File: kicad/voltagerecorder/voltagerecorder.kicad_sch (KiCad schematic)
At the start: 35 parts

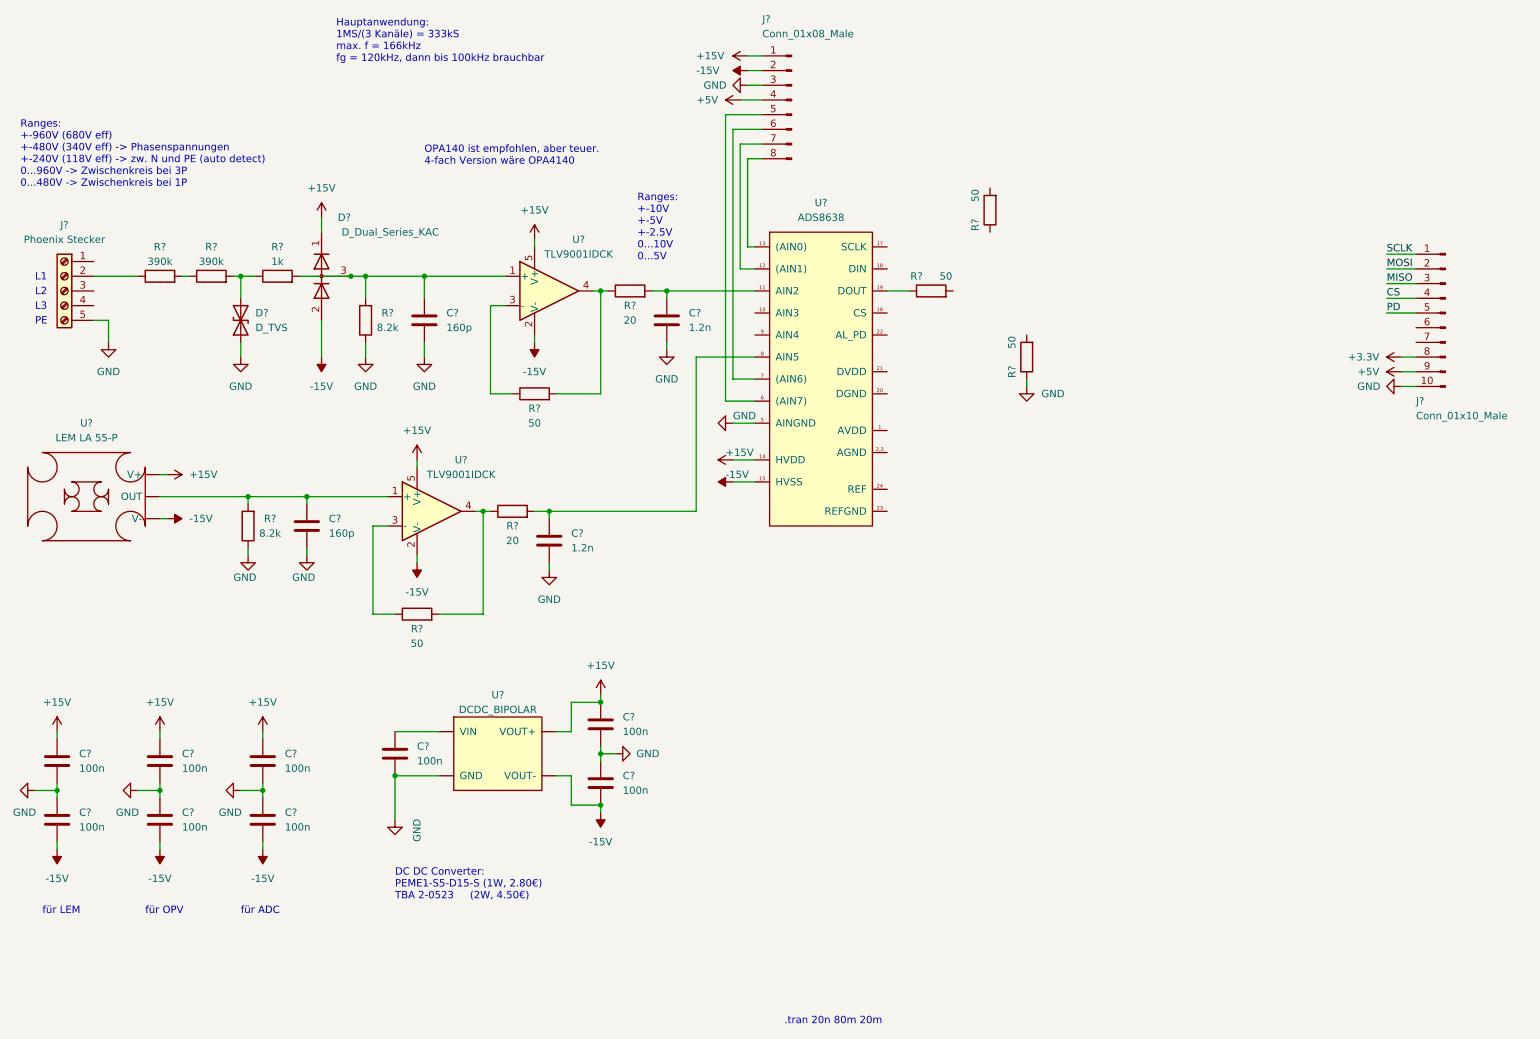
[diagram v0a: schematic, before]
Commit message: Schaltplan auf Hierachisch umgestellt.
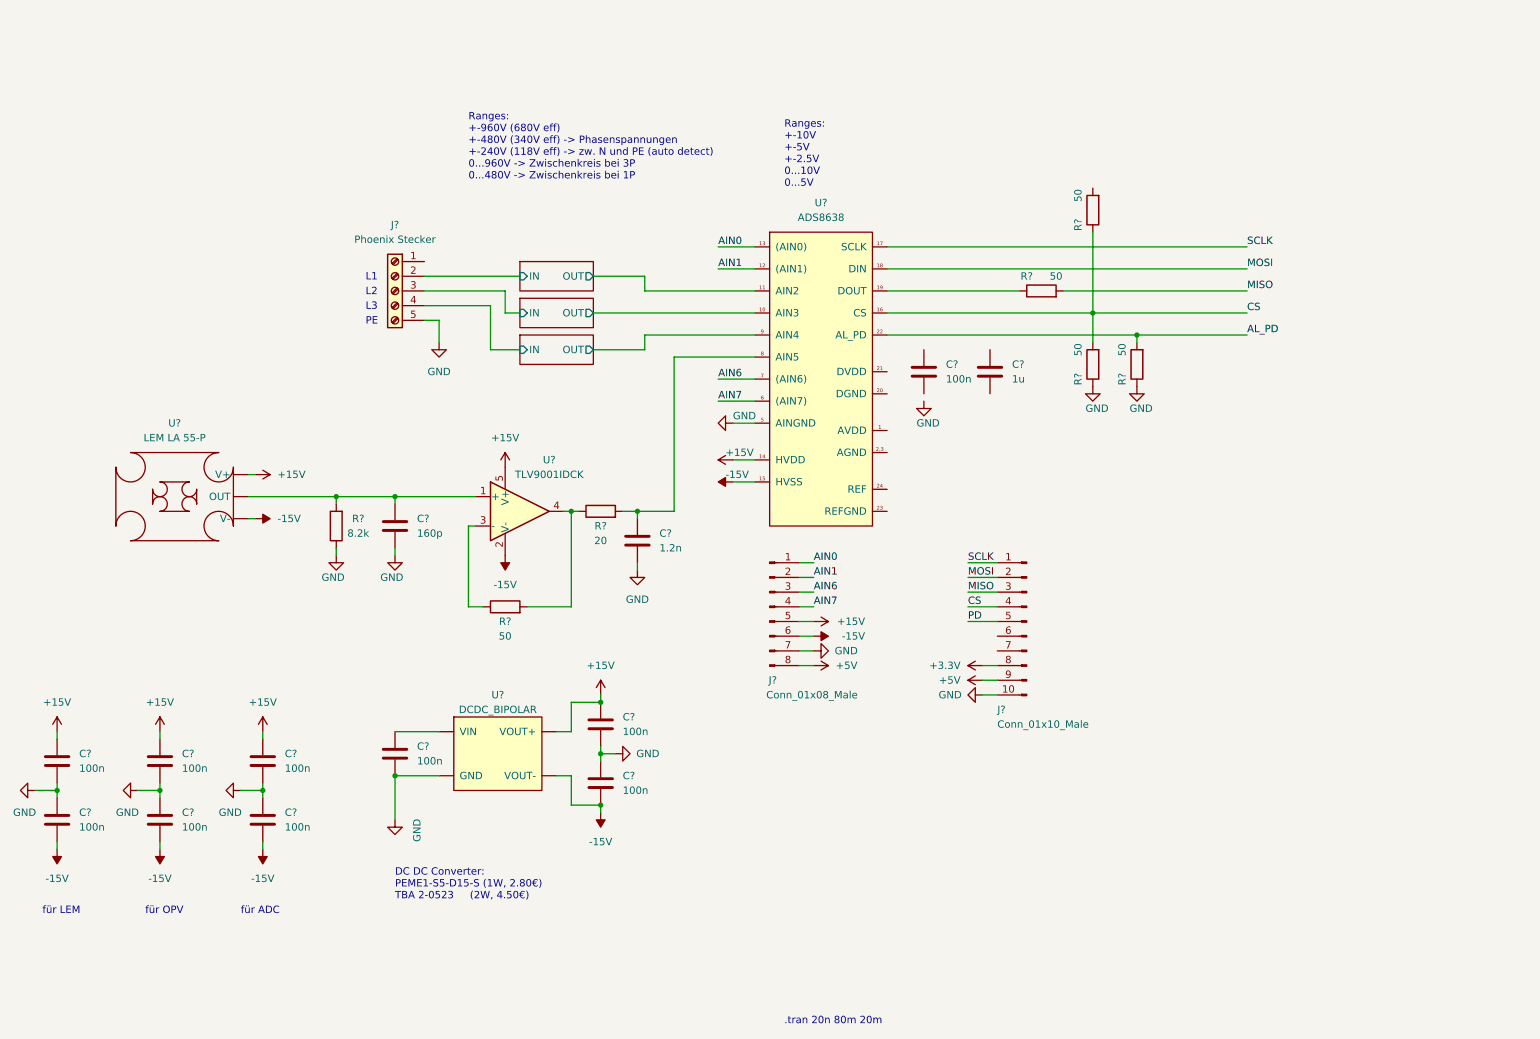
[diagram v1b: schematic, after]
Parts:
- removed C?: 1.2n, symbol Device:C
- removed C?: 160p, symbol Device:C
- removed D?: D_Dual_Series_KAC, symbol Device:D_Dual_Series_KAC
- removed D?: D_TVS, symbol Device:D_TVS
- removed R?: 8.2k, symbol Device:R
- removed R?: 20, symbol Device:R
- removed R?: 1k, symbol Device:R
- removed R? (x2): 390k, symbol Device:R
- removed R?: 50, symbol Device:R
- removed U?: TLV9001IDCK, Package_TO_SOT_SMD:SOT-353_SC-70-5, symbol Amplifier_Operational:TLV9001IDCK
- added C?: 1u, symbol Device:C
- added C?: 100n, symbol Device:C
- added R?: 50, symbol Device:R
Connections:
- net +15V: now also J?.5 (Pin_5); no longer J?.1 (Pin_1)
- net +5V: now also J?.8 (Pin_8); no longer J?.4 (Pin_4)
- net -15V: now also J?.6 (Pin_6); no longer J?.2 (Pin_2)
- net CS: now also R?.1, U?.16 (CS), R?.2
- net GND: now also J?.7 (Pin_7), R?.1; no longer J?.3 (Pin_3)
- net MISO: now also R?.2
- net MOSI: now also U?.18 (DIN)
- net SCLK: now also U?.17 (SCLK)
- net voltage_input/OUT: now reaches U?.11 (AIN2)
- net voltage_input/IN: now reaches J?.2 (Pin_2)
- net voltage_input1/IN: now reaches J?.3 (Pin_3)
- net voltage_input2/IN: now reaches J?.4 (Pin_4)
- net AL_PD: now reaches R?.2
- net AL_PD: now also U?.22 (AL_PD)
- net AIN7: now reaches U?.6 ((AIN7))
- net AIN7: now also J?.4 (Pin_4); no longer J?.5 (Pin_5)
- net AIN6: now reaches U?.7 ((AIN6))
- net AIN6: now also J?.3 (Pin_3); no longer J?.6 (Pin_6)
- net AIN1: now reaches U?.12 ((AIN1))
- net AIN1: now also J?.2 (Pin_2); no longer J?.7 (Pin_7)
- net AIN0: now reaches U?.13 ((AIN0))
- net AIN0: now also J?.1 (Pin_1); no longer J?.8 (Pin_8)
- net voltage_input1/OUT: now reaches U?.10 (AIN3)
- net voltage_input2/OUT: now reaches U?.9 (AIN4)
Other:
- added sheet voltage_input (voltage_input.kicad_sch)
- added sheet voltage_input1 (voltage_input.kicad_sch)
- added sheet voltage_input2 (voltage_input.kicad_sch)
- note removed: "Hauptanwendung: 1MS/(3 Kanäle) = 333kS max. f = 166kHz fg = 120kHz, dann bis 100kHz brauchbar"
- note removed: "OPA140 ist empfohlen, aber teuer. 4-fach Version wäre OPA4140"
- moved on the sheet: C?, J?, R?, U?

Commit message: Nach Aufteilung auf Hierachische Schaltpläne.
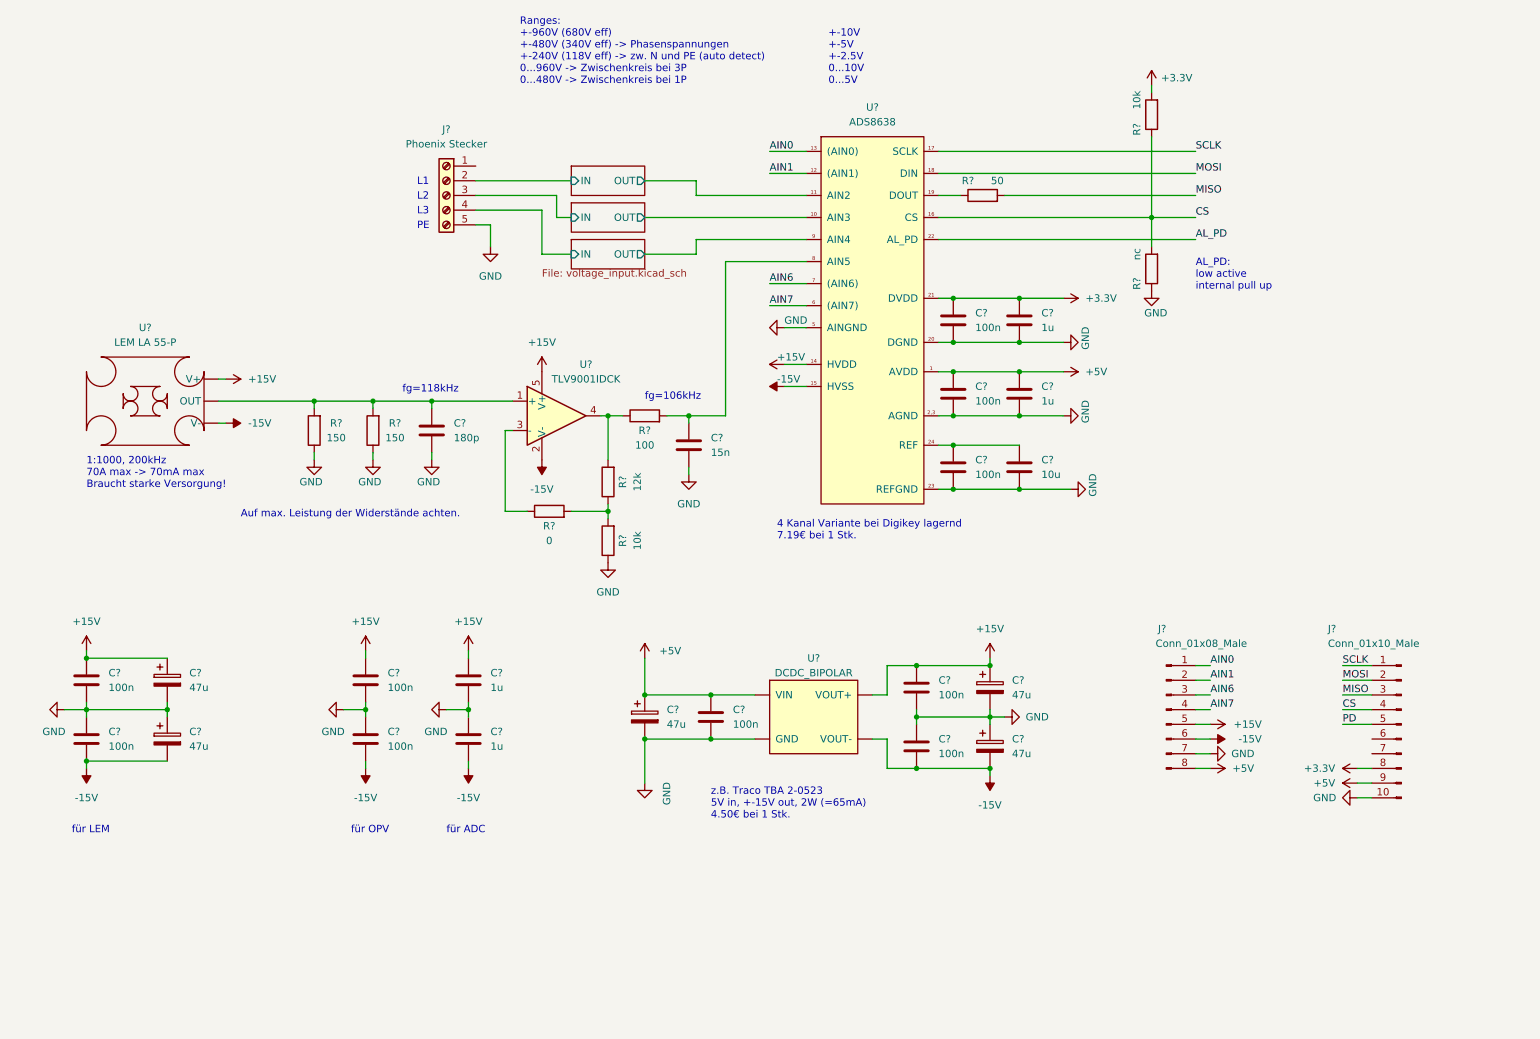
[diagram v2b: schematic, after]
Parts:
- removed R?: 50, symbol Device:R
- added C? (x2): 100n, symbol Device:C
- added C? (x5): 47u, symbol Device:C_Polarized
- added C?: 1u, symbol Device:C
- added C?: 10u, symbol Device:C
- added R?: 12k, symbol Device:R
- added R?: 150, symbol Device:R
- added R?: 10k, symbol Device:R
- C?: value 1.2n -> 15n
- C? (x2): value 100n -> 1u
- C?: value 160p -> 180p
- R?: value 50 -> 10k
- R?: value 50 -> nc
- R?: value 50 -> 0
- R?: value 20 -> 100
- R?: value 8.2k -> 150
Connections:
- net +15V: now also C?.1, C?.1
- net +3.3V: now also C?.1, C?.1, R?.2, U?.21 (DVDD)
- net +5V: now also C?.1, U?. (VOUT-), U?.1 (AVDD), C?.1, C?.1, C?.1
- net -15V: now also C?.2, C?.2
- net GND: now also C?.2, C?.2, U?.2,3 (AGND), U?.20 (DGND), U?.23 (REFGND), C?.1, C?.1, C?.2, C?.2, C?.2, C?.2, C?.2, C?.2, C?.2, R?.1, R?.1
- net at C?.1, R?.2, U?. (V-)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: now also R?.2
- net at R?.1, U?.4: now also R?.2; no longer R?.2
- net at U?.24 (REF): now also C?.1, C?.1
- new net: R?.1, R?.2, R?.2
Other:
- note added: "+-10V +-5V +-2.5V 0...10V 0...5V"
- note added: "1:1000, 200kHz 70A max -> 70mA max Braucht starke Versorgung!"
- note added: "4 Kanal Variante bei Digikey lagernd 7.19€ bei 1 Stk."
- note added: "AL_PD: low active internal pull up"
- note added: "Auf max. Leistung der Widerstände achten."
- note added: "fg=106kHz"
- note added: "fg=118kHz"
- note added: "z.B. Traco TBA 2-0523 5V in, +-15V out, 2W (=65mA) 4.50€ bei 1 Stk."
- note removed: ".tran 20n 80m 20m"
- note removed: "DC DC Converter: PEME1-S5-D15-S (1W, 2.80€) TBA 2-0523 (2W, 4.50€)"
- note removed: "Ranges: +-10V +-5V +-2.5V 0...10V 0...5V"
- moved on the sheet: C?, J?, R?, U?

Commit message: filters changed
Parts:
- C?: value 15n -> 8.2n
- C?: value 180p -> 100p
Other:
- note added: "194kHz"
- note added: "212kHz"
- note removed: "fg=106kHz"
- note removed: "fg=118kHz"

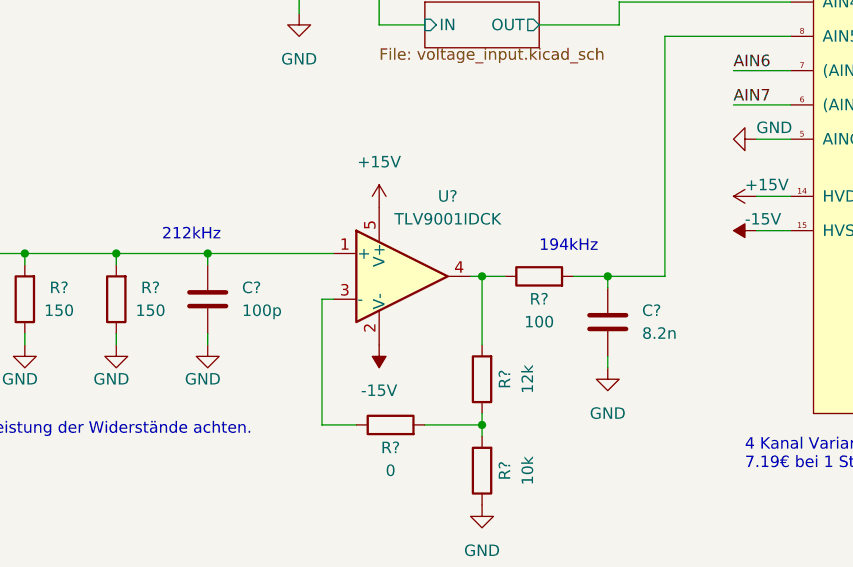
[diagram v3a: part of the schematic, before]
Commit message: Schematic as pdf added.
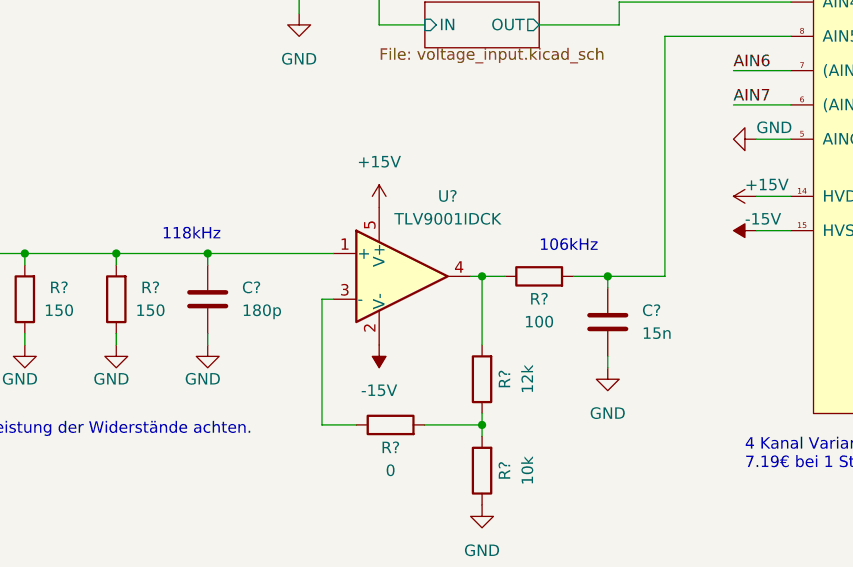
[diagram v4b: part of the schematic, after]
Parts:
- C?: value 8.2n -> 15n
- C?: value 100p -> 180p
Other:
- note added: "106kHz"
- note added: "118kHz"
- note removed: "194kHz"
- note removed: "212kHz"

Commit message: BOM hinzugefügt, Schaltplan editiert.
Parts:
- R?: value 12k -> 27k
- R?: value 50 -> 100
